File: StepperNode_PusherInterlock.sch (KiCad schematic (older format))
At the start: 12 parts

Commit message: First Revision -
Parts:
- removed P? (x2): CONN_01X08_2MNT, symbol CONN_01X08_2MNT
- added P4, P5: TE_640456-8, RLOOP_FOOTPRINTS:rLoop_TE640456-8, symbol TE_640456-8
- gave numbers to parts that had none: 10
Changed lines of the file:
@@
 Text Notes 11950 10500 0    60   ~ 0
 Original Author: SafetyLok
-$Comp
-L CONN_01X08_2MNT P?
-U 1 1 575DC45D
-P 13050 3050
-F 0 "P?" H 13050 3500 50  0000 C CNN
-F 1 "CONN_01X08_2MNT" V 13150 3050 50  0000 C CNN
-F 2 "" H 13050 3050 50  0000 C CNN
-F 3 "" H 13050 3050 50  0000 C CNN
-	1    13050 3050
-	1    0    0    -1
-$EndComp
 Text Notes 13500 3550 1    60   ~ 0
 Gimbal Switch Interfaces
 $Comp
-L GNDD #PWR?
+L GNDD #PWR33
 U 1 1 575DC471
 P 12650 3500
-F 0 "#PWR?" H 12650 3250 50  0001 C CNN
+F 0 "#PWR33" H 12650 3250 50  0001 C CNN
 F 1 "GNDD" H 12650 3350 50  0000 C CNN
 F 2 "" H 12650 3500 50  0000 C CNN
@@
 Wire Wire Line
 	11750 3200 12850 3200
-$Comp
-L CONN_01X08_2MNT P?
-U 1 1 575DC483
-P 13050 4450
-F 0 "P?" H 13050 4900 50  0000 C CNN
-F 1 "CONN_01X08_2MNT" V 13150 4450 50  0000 C CNN
-F 2 "" H 13050 4450 50  0000 C CNN
-F 3 "" H 13050 4450 50  0000 C CNN
-	1    13050 4450
-	1    0    0    -1
-$EndComp
 Text Notes 13500 4950 1    60   ~ 0
 Gimbal Switch Interfaces
 $Comp
-L GNDD #PWR?
+L GNDD #PWR34
 U 1 1 575DC497
 P 12650 4900
-F 0 "#PWR?" H 12650 4650 50  0001 C CNN
+F 0 "#PWR34" H 12650 4650 50  0001 C CNN
 F 1 "GNDD" H 12650 4750 50  0000 C CNN
 F 2 "" H 12650 4900 50  0000 C CNN
@@
 	11750 4600 12850 4600
 $Comp
-L GNDD #PWR?
+L GNDD #PWR28
 U 1 1 575DC4D0
 P 5300 5100
-F 0 "#PWR?" H 5300 4850 50  0001 C CNN
+F 0 "#PWR28" H 5300 4850 50  0001 C CNN
 F 1 "GNDD" H 5300 4950 50  0000 C CNN
 F 2 "" H 5300 5100 50  0000 C CNN
@@
 	5650 5100 5650 4800
 $Comp
-L +3V3_A #PWR?
+L +3V3_A #PWR27
 U 1 1 575DC4D8
 P 5300 2450
-F 0 "#PWR?" H 5300 2300 50  0001 C CNN
+F 0 "#PWR27" H 5300 2300 50  0001 C CNN
 F 1 "+3V3_A" H 5300 2590 50  0000 C CNN
 F 2 "" H 5300 2450 60  0000 C CNN
@@
 	4550 3650 4550 3450
 $Comp
-L GNDD #PWR?
+L GNDD #PWR25
 U 1 1 575DC4E6
 P 4950 3900
-F 0 "#PWR?" H 4950 3650 50  0001 C CNN
+F 0 "#PWR25" H 4950 3650 50  0001 C CNN
 F 1 "GNDD" H 4950 3750 50  0000 C CNN
 F 2 "" H 4950 3900 50  0000 C CNN
@@
 	6400 3900 7550 3900
 $Comp
-L GNDD #PWR?
+L GNDD #PWR31
 U 1 1 575DC71B
 P 6400 4300
-F 0 "#PWR?" H 6400 4050 50  0001 C CNN
+F 0 "#PWR31" H 6400 4050 50  0001 C CNN
 F 1 "GNDD" H 6400 4150 50  0000 C CNN
 F 2 "" H 6400 4300 50  0000 C CNN
@@
 PSH_1_RETURN
 $Comp
-L +3V3_A #PWR?
+L +3V3_A #PWR23
 U 1 1 575DCA53
 P 4100 3950
-F 0 "#PWR?" H 4100 3800 50  0001 C CNN
+F 0 "#PWR23" H 4100 3800 50  0001 C CNN
 F 1 "+3V3_A" H 4100 4090 50  0000 C CNN
 F 2 "" H 4100 3950 60  0000 C CNN
@@
 PUSH_INTLK_B
 $Comp
-L GNDD #PWR?
+L GNDD #PWR30
 U 1 1 575DCF10
 P 5300 8900
-F 0 "#PWR?" H 5300 8650 50  0001 C CNN
+F 0 "#PWR30" H 5300 8650 50  0001 C CNN
 F 1 "GNDD" H 5300 8750 50  0000 C CNN
 F 2 "" H 5300 8900 50  0000 C CNN
@@
 	5650 8900 5650 8600
 $Comp
-L +3V3_A #PWR?
+L +3V3_A #PWR29
 U 1 1 575DCF18
 P 5300 6250
-F 0 "#PWR?" H 5300 6100 50  0001 C CNN
+F 0 "#PWR29" H 5300 6100 50  0001 C CNN
 F 1 "+3V3_A" H 5300 6390 50  0000 C CNN
 F 2 "" H 5300 6250 60  0000 C CNN
@@
 	4550 7450 4550 7250
 $Comp
-L GNDD #PWR?
+L GNDD #PWR26
 U 1 1 575DCF26
 P 4950 7700
-F 0 "#PWR?" H 4950 7450 50  0001 C CNN
+F 0 "#PWR26" H 4950 7450 50  0001 C CNN
 F 1 "GNDD" H 4950 7550 50  0000 C CNN
 F 2 "" H 4950 7700 50  0000 C CNN
@@
 	6400 7700 7550 7700
 $Comp
-L GNDD #PWR?
+L GNDD #PWR32
 U 1 1 575DCF2E
 P 6400 8100
-F 0 "#PWR?" H 6400 7850 50  0001 C CNN
+F 0 "#PWR32" H 6400 7850 50  0001 C CNN
 F 1 "GNDD" H 6400 7950 50  0000 C CNN
 F 2 "" H 6400 8100 50  0000 C CNN
@@
 	4100 7800 4100 7750
 $Comp
-L +3V3_A #PWR?
+L +3V3_A #PWR24
 U 1 1 575DD2D6
 P 4100 7750
-F 0 "#PWR?" H 4100 7600 50  0001 C CNN
+F 0 "#PWR24" H 4100 7600 50  0001 C CNN
 F 1 "+3V3_A" H 4100 7890 50  0000 C CNN
 F 2 "" H 4100 7750 60  0000 C CNN
@@
 PSH_2_RETURN
 $Comp
-L MAX3232CDR U?
+L MAX3232CDR U4
 U 1 1 575A130F
 P 5150 2950
-F 0 "U?" H 6150 3050 60  0000 C CNN
+F 0 "U4" H 6150 3050 60  0000 C CNN
 F 1 "MAX3232CDR" H 6000 1250 60  0000 C CNN
 F 2 "RLOOP_FOOTPRINTS:rLoop_SOIC_16" H 5350 2350 60  0001 C CNN
@@
 $EndComp
 $Comp
-L MAX3232CDR U?
+L MAX3232CDR U5
 U 1 1 575A140C
 P 5150 6750
-F 0 "U?" H 6150 6850 60  0000 C CNN
+F 0 "U5" H 6150 6850 60  0000 C CNN
 F 1 "MAX3232CDR" H 6000 5050 60  0000 C CNN
 F 2 "RLOOP_FOOTPRINTS:rLoop_SOIC_16" H 5350 6150 60  0001 C CNN
@@
 $EndComp
 $Comp
-L C_100nF_50V C?
+L C_100nF_50V C10
 U 1 1 575A15C1
 P 5300 6400
-F 0 "C?" H 5325 6500 50  0000 L CNN
+F 0 "C10" H 5325 6500 50  0000 L CNN
 F 1 "C_100nF_50V" H 5325 6300 50  0000 L CNN
 F 2 "RLOOP_FOOTPRINTS:rLoop_C_0603" H 5338 6250 50  0001 C CNN
@@
 $EndComp
 $Comp
-L C_100nF_50V C?
+L C_100nF_50V C6
 U 1 1 575A1648
 P 4700 6950
-F 0 "C?" H 4725 7050 50  0000 L CNN
+F 0 "C6" H 4725 7050 50  0000 L CNN
 F 1 "C_100nF_50V" H 4725 6850 50  0000 L CNN
 F 2 "RLOOP_FOOTPRINTS:rLoop_C_0603" H 4738 6800 50  0001 C CNN
@@
 $EndComp
 $Comp
-L C_100nF_50V C?
+L C_100nF_50V C11
 U 1 1 575A16FF
 P 5300 8750
-F 0 "C?" H 5325 8850 50  0000 L CNN
+F 0 "C11" H 5325 8850 50  0000 L CNN
 F 1 "C_100nF_50V" H 5325 8650 50  0000 L CNN
 F 2 "RLOOP_FOOTPRINTS:rLoop_C_0603" H 5338 8600 50  0001 C CNN
@@
 $EndComp
 $Comp
-L C_100nF_50V C?
+L C_100nF_50V C9
 U 1 1 575A189E
 P 5300 4950
-F 0 "C?" H 5325 5050 50  0000 L CNN
+F 0 "C9" H 5325 5050 50  0000 L CNN
 F 1 "C_100nF_50V" H 5325 4850 50  0000 L CNN
 F 2 "RLOOP_FOOTPRINTS:rLoop_C_0603" H 5338 4800 50  0001 C CNN
@@
 $EndComp
 $Comp
-L C_100nF_50V C?
+L C_100nF_50V C8
 U 1 1 575A1A4C
 P 5300 2600
-F 0 "C?" H 5325 2700 50  0000 L CNN
+F 0 "C8" H 5325 2700 50  0000 L CNN
 F 1 "C_100nF_50V" H 5325 2500 50  0000 L CNN
 F 2 "RLOOP_FOOTPRINTS:rLoop_C_0603" H 5338 2450 50  0001 C CNN
@@
 $EndComp
 $Comp
-L C_100nF_50V C?
+L C_100nF_50V C7
 U 1 1 575A1C14
 P 4700 7250
-F 0 "C?" H 4725 7350 50  0000 L CNN
+F 0 "C7" H 4725 7350 50  0000 L CNN
 F 1 "C_100nF_50V" H 4725 7150 50  0000 L CNN
 F 2 "RLOOP_FOOTPRINTS:rLoop_C_0603" H 4738 7100 50  0001 C CNN
@@
 $EndComp
 $Comp
-L C_100nF_50V C?
+L C_100nF_50V C4
 U 1 1 575A1F38
 P 4700 3150
-F 0 "C?" H 4725 3250 50  0000 L CNN
+F 0 "C4" H 4725 3250 50  0000 L CNN
 F 1 "C_100nF_50V" H 4725 3050 50  0000 L CNN
 F 2 "RLOOP_FOOTPRINTS:rLoop_C_0603" H 4738 3000 50  0001 C CNN
@@
 $EndComp
 $Comp
-L C_100nF_50V C?
+L C_100nF_50V C5
 U 1 1 575A1FCB
 P 4700 3450
-F 0 "C?" H 4725 3550 50  0000 L CNN
+F 0 "C5" H 4725 3550 50  0000 L CNN
 F 1 "C_100nF_50V" H 4725 3350 50  0000 L CNN
 F 2 "RLOOP_FOOTPRINTS:rLoop_C_0603" H 4738 3300 50  0001 C CNN
@@
 	0    1    1    0
 $EndComp
+$Comp
+L TE_640456-8 P4
+U 1 1 57657663
+P 13000 2750
+F 0 "P4" H 13050 2800 50  0000 C CNN
+F 1 "TE_640456-8" V 13150 2350 50  0000 C CNN
+F 2 "RLOOP_FOOTPRINTS:rLoop_TE640456-8" H 13050 2350 50  0001 C CNN
+F 3 "" H 13050 2350 50  0000 C CNN
+	1    13000 2750
+	1    0    0    -1
+$EndComp
+$Comp
+L TE_640456-8 P5
+U 1 1 576576D6
+P 13000 4150
+F 0 "P5" H 13050 4200 50  0000 C CNN
+F 1 "TE_640456-8" V 13150 3750 50  0000 C CNN
+F 2 "RLOOP_FOOTPRINTS:rLoop_TE640456-8" H 13050 3750 50  0001 C CNN
+F 3 "" H 13050 3750 50  0000 C CNN
+	1    13000 4150
+	1    0    0    -1
+$EndComp
 $EndSCHEMATC

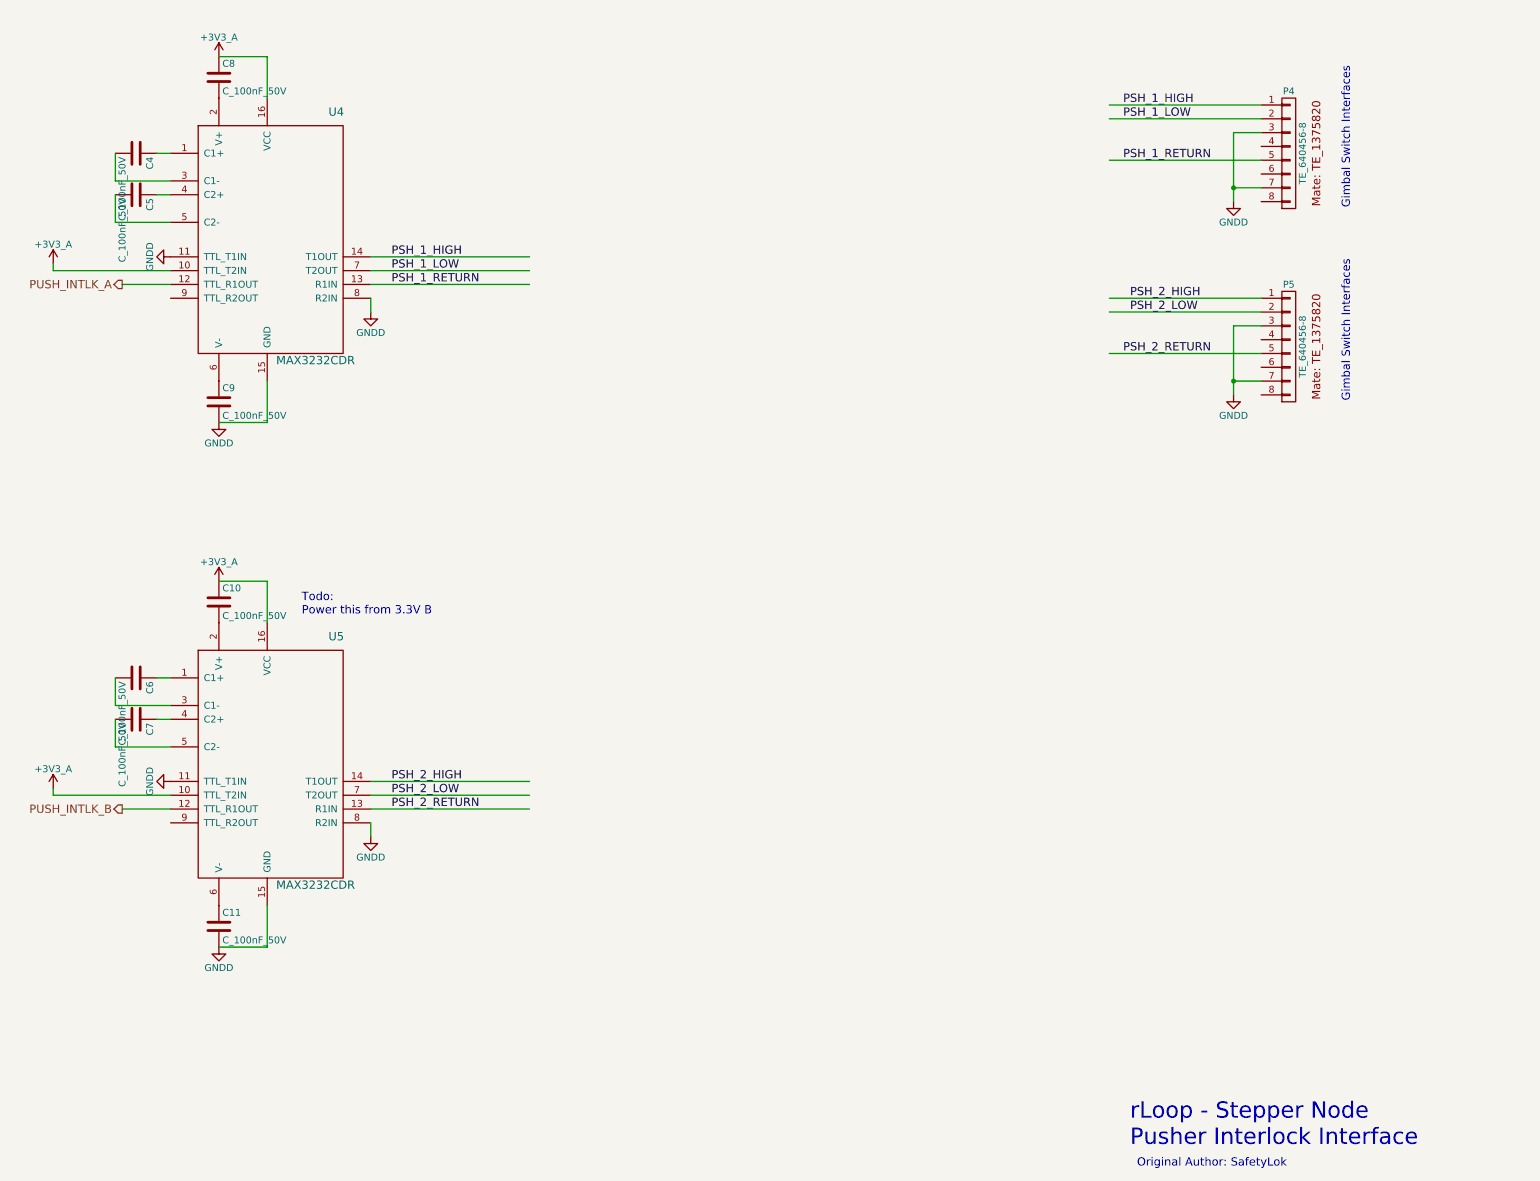
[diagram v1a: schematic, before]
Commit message: Fix most ERC warnings (non-connected pins, etc)
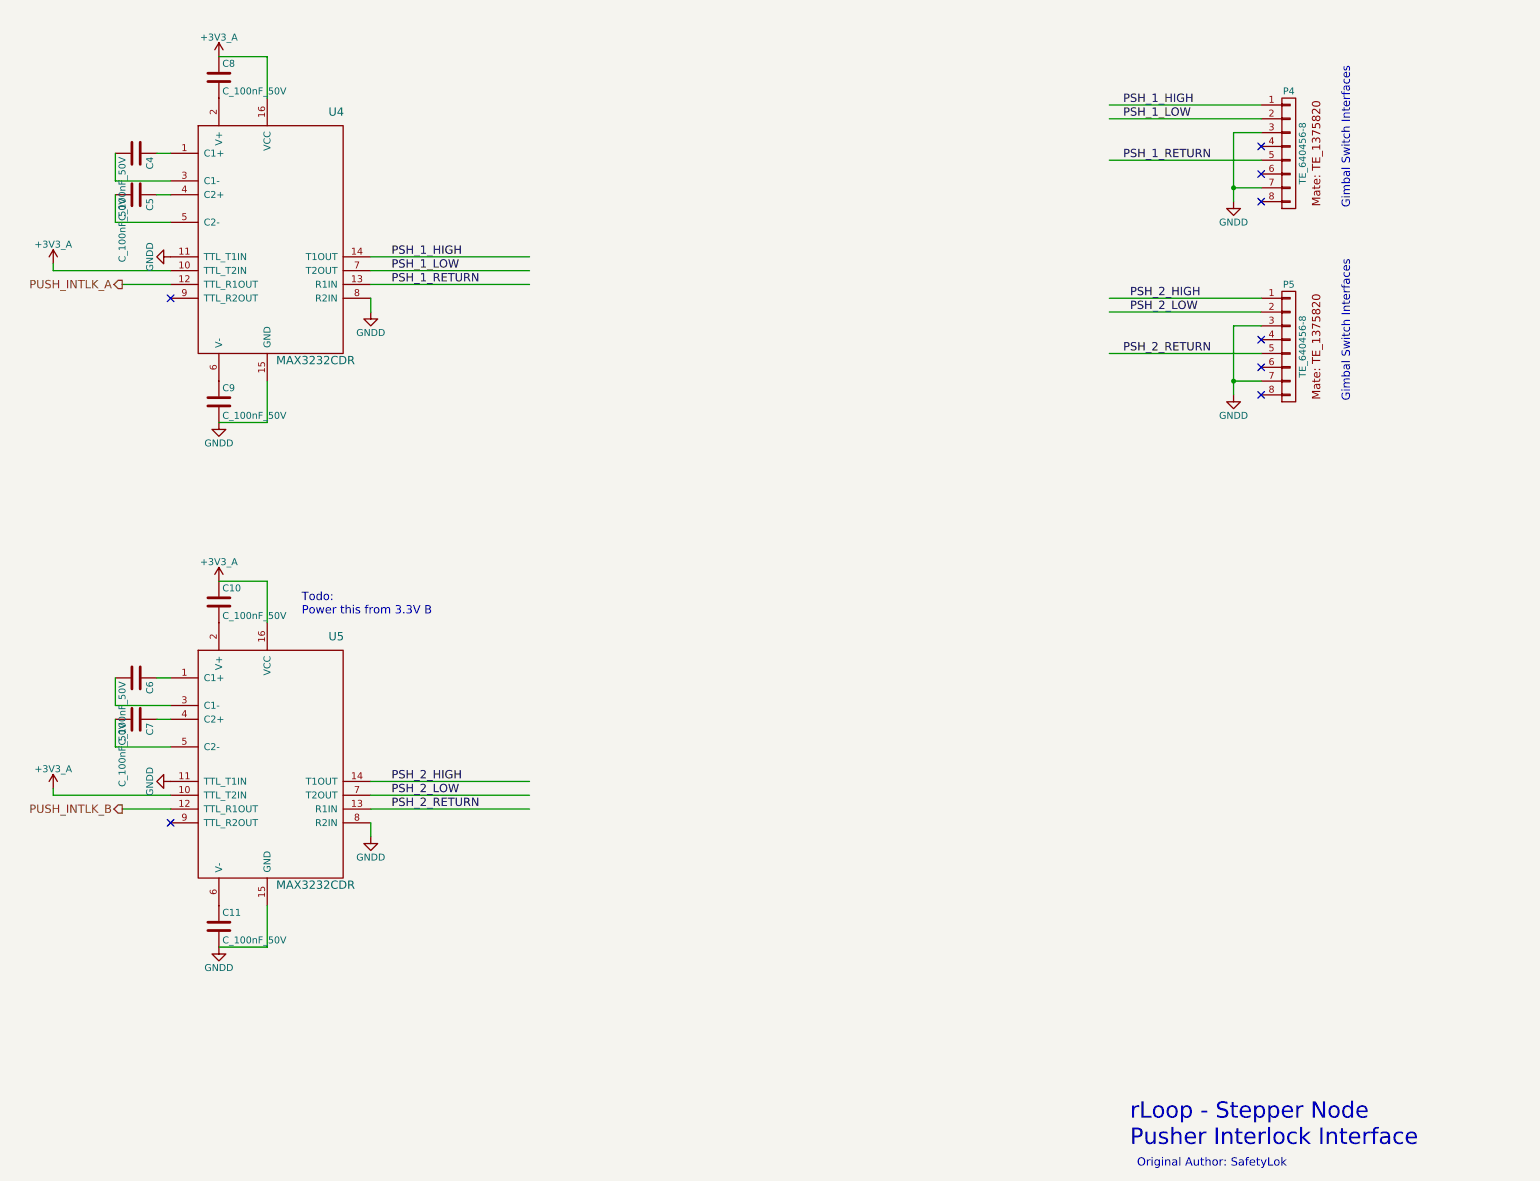
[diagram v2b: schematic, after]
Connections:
- no-connect marks 0 -> 8
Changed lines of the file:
@@
 Gimbal Switch Interfaces
 $Comp
-L GNDD #PWR33
+L GNDD #PWR025
 U 1 1 575DC471
 P 12650 3500
-F 0 "#PWR33" H 12650 3250 50  0001 C CNN
+F 0 "#PWR025" H 12650 3250 50  0001 C CNN
 F 1 "GNDD" H 12650 3350 50  0000 C CNN
 F 2 "" H 12650 3500 50  0000 C CNN
@@
 Gimbal Switch Interfaces
 $Comp
-L GNDD #PWR34
+L GNDD #PWR026
 U 1 1 575DC497
 P 12650 4900
-F 0 "#PWR34" H 12650 4650 50  0001 C CNN
+F 0 "#PWR026" H 12650 4650 50  0001 C CNN
 F 1 "GNDD" H 12650 4750 50  0000 C CNN
 F 2 "" H 12650 4900 50  0000 C CNN
@@
 	11750 4600 12850 4600
 $Comp
-L GNDD #PWR28
+L GNDD #PWR027
 U 1 1 575DC4D0
 P 5300 5100
-F 0 "#PWR28" H 5300 4850 50  0001 C CNN
+F 0 "#PWR027" H 5300 4850 50  0001 C CNN
 F 1 "GNDD" H 5300 4950 50  0000 C CNN
 F 2 "" H 5300 5100 50  0000 C CNN
@@
 	5650 5100 5650 4800
 $Comp
-L +3V3_A #PWR27
+L +3V3_A #PWR028
 U 1 1 575DC4D8
 P 5300 2450
-F 0 "#PWR27" H 5300 2300 50  0001 C CNN
+F 0 "#PWR028" H 5300 2300 50  0001 C CNN
 F 1 "+3V3_A" H 5300 2590 50  0000 C CNN
 F 2 "" H 5300 2450 60  0000 C CNN
@@
 	4550 3650 4550 3450
 $Comp
-L GNDD #PWR25
+L GNDD #PWR029
 U 1 1 575DC4E6
 P 4950 3900
-F 0 "#PWR25" H 4950 3650 50  0001 C CNN
+F 0 "#PWR029" H 4950 3650 50  0001 C CNN
 F 1 "GNDD" H 4950 3750 50  0000 C CNN
 F 2 "" H 4950 3900 50  0000 C CNN
@@
 	6400 3900 7550 3900
 $Comp
-L GNDD #PWR31
+L GNDD #PWR030
 U 1 1 575DC71B
 P 6400 4300
-F 0 "#PWR31" H 6400 4050 50  0001 C CNN
+F 0 "#PWR030" H 6400 4050 50  0001 C CNN
 F 1 "GNDD" H 6400 4150 50  0000 C CNN
 F 2 "" H 6400 4300 50  0000 C CNN
@@
 PSH_1_RETURN
 $Comp
-L +3V3_A #PWR23
+L +3V3_A #PWR031
 U 1 1 575DCA53
 P 4100 3950
-F 0 "#PWR23" H 4100 3800 50  0001 C CNN
+F 0 "#PWR031" H 4100 3800 50  0001 C CNN
 F 1 "+3V3_A" H 4100 4090 50  0000 C CNN
 F 2 "" H 4100 3950 60  0000 C CNN
@@
 PUSH_INTLK_B
 $Comp
-L GNDD #PWR30
+L GNDD #PWR032
 U 1 1 575DCF10
 P 5300 8900
-F 0 "#PWR30" H 5300 8650 50  0001 C CNN
+F 0 "#PWR032" H 5300 8650 50  0001 C CNN
 F 1 "GNDD" H 5300 8750 50  0000 C CNN
 F 2 "" H 5300 8900 50  0000 C CNN
@@
 	5650 8900 5650 8600
 $Comp
-L +3V3_A #PWR29
+L +3V3_A #PWR033
 U 1 1 575DCF18
 P 5300 6250
-F 0 "#PWR29" H 5300 6100 50  0001 C CNN
+F 0 "#PWR033" H 5300 6100 50  0001 C CNN
 F 1 "+3V3_A" H 5300 6390 50  0000 C CNN
 F 2 "" H 5300 6250 60  0000 C CNN
@@
 	4550 7450 4550 7250
 $Comp
-L GNDD #PWR26
+L GNDD #PWR034
 U 1 1 575DCF26
 P 4950 7700
-F 0 "#PWR26" H 4950 7450 50  0001 C CNN
+F 0 "#PWR034" H 4950 7450 50  0001 C CNN
 F 1 "GNDD" H 4950 7550 50  0000 C CNN
 F 2 "" H 4950 7700 50  0000 C CNN
@@
 	6400 7700 7550 7700
 $Comp
-L GNDD #PWR32
+L GNDD #PWR035
 U 1 1 575DCF2E
 P 6400 8100
-F 0 "#PWR32" H 6400 7850 50  0001 C CNN
+F 0 "#PWR035" H 6400 7850 50  0001 C CNN
 F 1 "GNDD" H 6400 7950 50  0000 C CNN
 F 2 "" H 6400 8100 50  0000 C CNN
@@
 	4100 7800 4100 7750
 $Comp
-L +3V3_A #PWR24
+L +3V3_A #PWR036
 U 1 1 575DD2D6
 P 4100 7750
-F 0 "#PWR24" H 4100 7600 50  0001 C CNN
+F 0 "#PWR036" H 4100 7600 50  0001 C CNN
 F 1 "+3V3_A" H 4100 7890 50  0000 C CNN
 F 2 "" H 4100 7750 60  0000 C CNN
@@
 	1    0    0    -1
 $EndComp
+NoConn ~ 4950 4200
+NoConn ~ 4950 8000
+NoConn ~ 12850 3100
+NoConn ~ 12850 3300
+NoConn ~ 12850 3500
+NoConn ~ 12850 4500
+NoConn ~ 12850 4700
+NoConn ~ 12850 4900
 $EndSCHEMATC
